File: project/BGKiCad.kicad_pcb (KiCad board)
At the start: 2 copper layers, 114.3 x 50.8 mm, 13 parts, among them J1 Alt. Power, J2 SWD, SW1 SW_Choc_v1_HS_CPG135001S30_Re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, SW2 SW_Choc_v1_HS_CPG135001S30_Re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, SW3 SW_Choc_v1_HS_CPG135001S30_Re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, SW4 SW_Choc_v1_HS_CPG135001S30_Re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, SW5 SW_Choc_v1_HS_CPG135001S30_Re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, SW6 SW_Choc_v1_HS_CPG135001S30_Re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

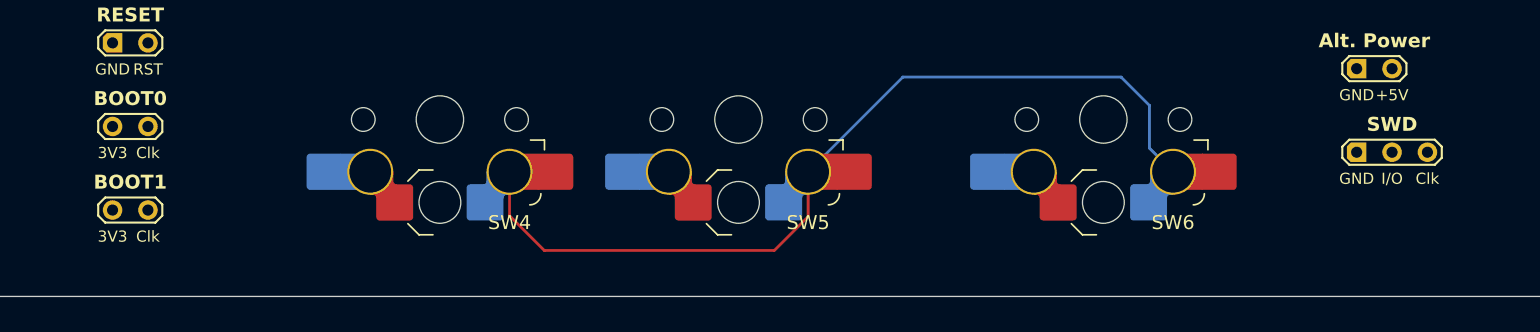
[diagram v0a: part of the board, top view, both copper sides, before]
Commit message: Make centre pad thermal connections 45º instead of 90º
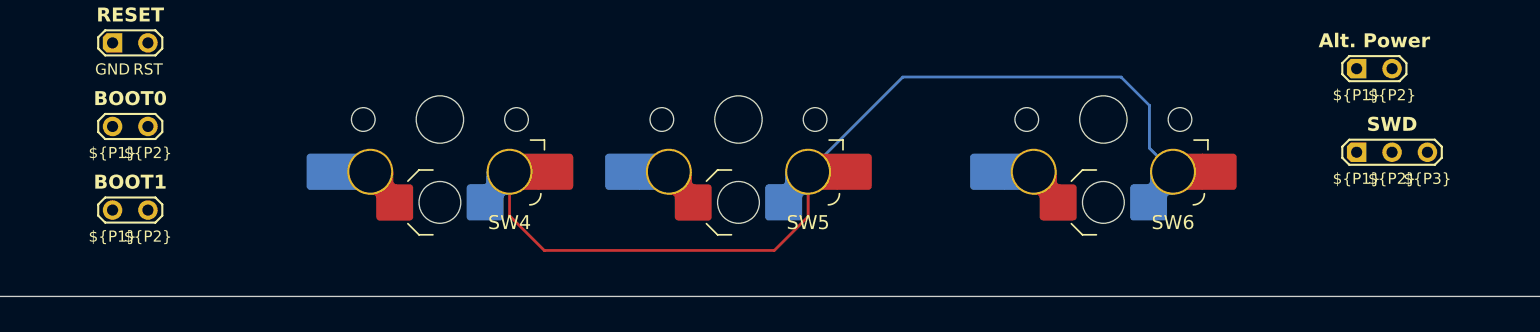
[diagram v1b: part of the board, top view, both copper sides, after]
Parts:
- SW1: value SW_Choc_v1_HS_CPG135001S30_Reversible_CtrPlt_1u -> CPG135001S30
- SW2: value SW_Choc_v1_HS_CPG135001S30_Reversible_CtrPlt_1.25u -> CPG135001S30
- SW3: value SW_Choc_v1_HS_CPG135001S30_Reversible_CtrPlt_1.5u -> CPG135001S30
- SW4: value SW_Choc_v1_HS_CPG135001S30_Reversible_OutPlt_1u -> CPG135001S30
- SW5: value SW_Choc_v1_HS_CPG135001S30_Reversible_OutPlt_1.25u -> CPG135001S30
- SW6: value SW_Choc_v1_HS_CPG135001S30_Reversible_OutPlt_1.5u -> CPG135001S30
